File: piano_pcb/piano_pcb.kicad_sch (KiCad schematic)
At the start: 13 parts, among them J1 DIN-6, J2 DIN-6, U1 TB6612FNG

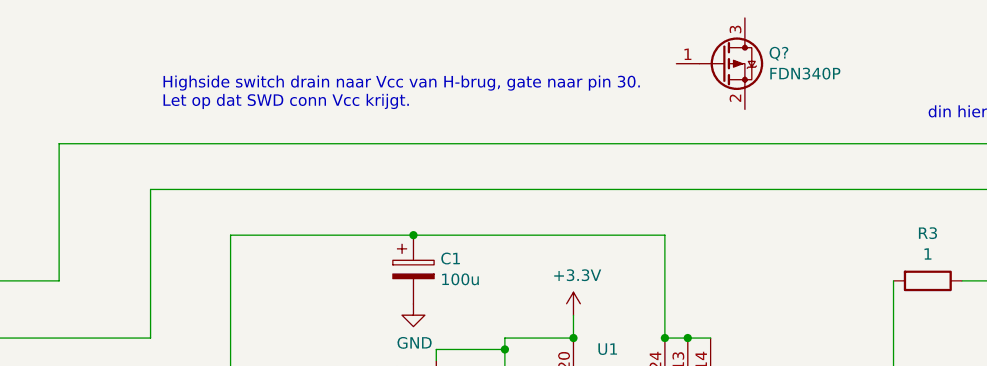
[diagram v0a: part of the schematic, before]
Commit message: Improved low power behaviour
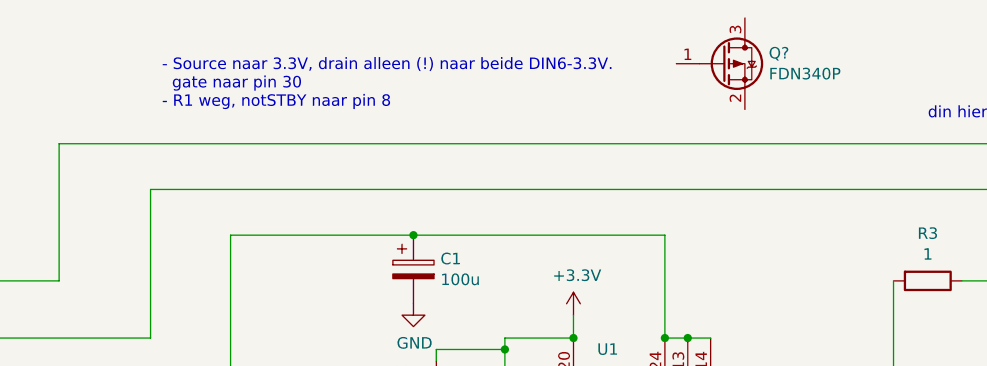
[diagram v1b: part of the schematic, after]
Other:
- note added: "- Source naar 3.3V, drain alleen (!) naar beide DIN6-3.3V. gate naar pin 30 - R1 weg, notSTBY naar pin 8"
- note removed: "Highside switch drain naar Vcc van H-brug, gate naar pin 30. Let op dat SWD conn Vcc krijgt."
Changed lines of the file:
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@@
     (effects (font (size 1.27 1.27)) (justify left bottom))
   )
-  (text "Highside switch drain naar Vcc van H-brug, gate naar pin 30.\nLet op dat SWD conn Vcc krijgt."
+  (text "- Source naar 3.3V, drain alleen (!) naar beide DIN6-3.3V.\n  gate naar pin 30\n- R1 weg, notSTBY naar pin 8"
     (at 158.75 25.4 0)
     (effects (font (size 1.27 1.27)) (justify left bottom))

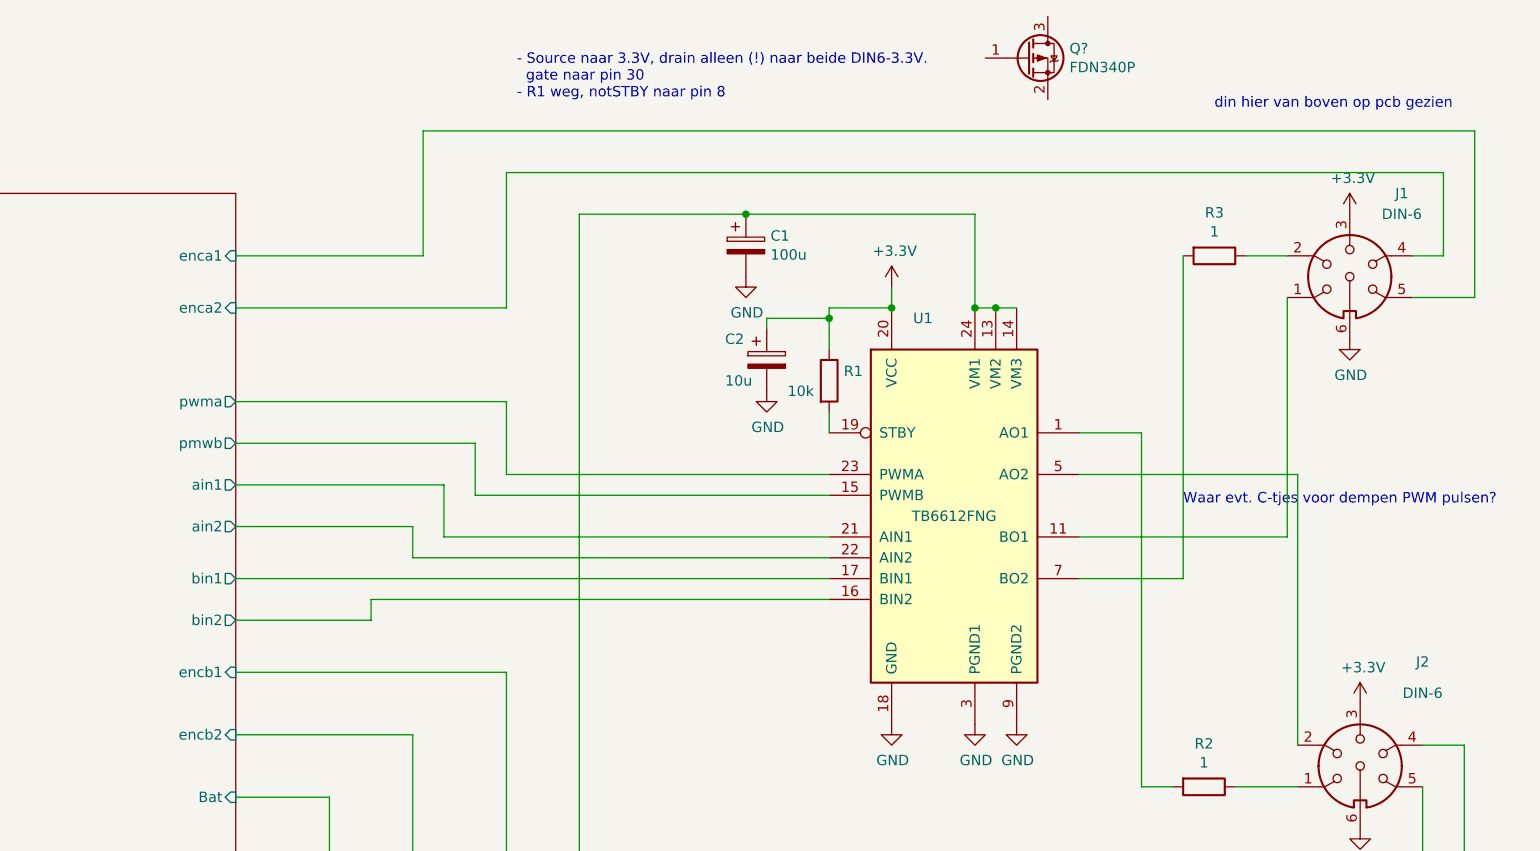
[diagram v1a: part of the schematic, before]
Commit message: Updated schematics, NOT PCB
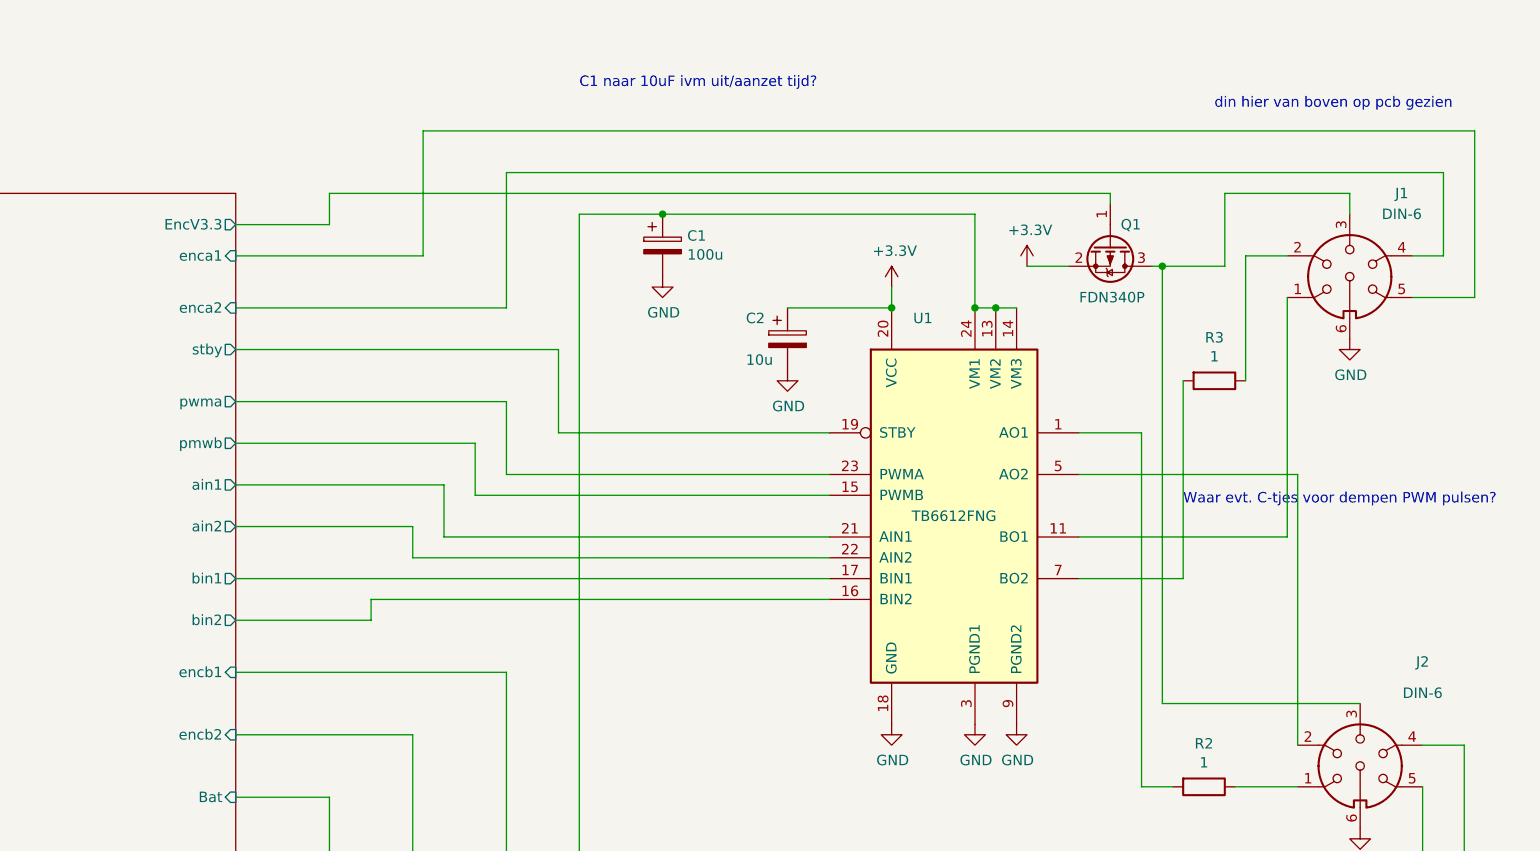
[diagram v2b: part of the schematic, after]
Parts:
- removed R1: 10k, Resistor_SMD:R_0805_2012Metric_Pad1.20x1.40mm_HandSolder, symbol Device:R
- gave numbers to parts that had none: 1
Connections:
- net +3V3: now also Q1.2 (S); no longer J1.3, J2.3
- net Controller/stby: now reaches U1.19 (STBY)
- net Controller/EncV3.3: now reaches Q1.1 (G)
- net at Q1.3 (D): now also J1.3, J2.3
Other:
- sheet Controller ports: added EncV3.3, stby; removed none
- note added: "C1 naar 10uF ivm uit/aanzet tijd?"
- note removed: "- Source naar 3.3V, drain alleen (!) naar beide DIN6-3.3V. gate naar pin 30 - R1 weg, notSTBY naar pin 8"
- moved on the sheet: C1, C2, Q1, R3

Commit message: Minor updates
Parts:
- C1: value 100u -> 10u
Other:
- note added: "Aan welke kant moet de USB plug?"
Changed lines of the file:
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@@
+    (effects (font (size 1.27 1.27)) (justify left bottom))
+  )
+  (text "Aan welke kant moet de USB plug?" (at 62.23 24.13 0)
     (effects (font (size 1.27 1.27)) (justify left bottom))
   )
@@
       (effects (font (size 1.27 1.27)) (justify left))
     )
-    (property "Value" "100u" (id 1) (at 179.5272 44.323 0)
+    (property "Value" "10u" (id 1) (at 179.5272 44.323 0)
       (effects (font (size 1.27 1.27)) (justify left))
     )
@@
     )
     (path "/00000000-0000-0000-0000-00006054c04d"
-      (reference "C1") (unit 1) (value "100u") (footprint "Capacitor_Tantalum_SMD:CP_EIA-7343-30_AVX-N_Pad2.25x2.55mm_HandSolder")
+      (reference "C1") (unit 1) (value "10u") (footprint "Capacitor_Tantalum_SMD:CP_EIA-7343-30_AVX-N_Pad2.25x2.55mm_HandSolder")
     )
     (path "/00000000-0000-0000-0000-00006054c997"
@@
       (reference "J6") (unit 1) (value "Conn_02x01") (footprint "Connector_PinHeader_2.54mm:PinHeader_1x02_P2.54mm_Vertical")
     )
+    (path "/00000000-0000-0000-0000-00006048eab7/0ba958be-8911-456e-aad0-fe6eb7697cab"
+      (reference "J7") (unit 1) (value "Conn_01x02") (footprint "TerminalBlock_Altech:Altech_AK300_1x02_P5.00mm_45-Degree")
+    )
     (path "/00000000-0000-0000-0000-0000632247d1"

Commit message: Optimized for low power
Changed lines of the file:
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@@
 (kicad_sch
-	(version 20231120)
+	(version 20250114)
 	(generator "eeschema")
-	(generator_version "8.0")
+	(generator_version "9.0")
 	(paper "A4")
 	(title_block
@@
 		(comment 4 "Author: Sietse Achterop")
 	)
+	(text "din hier van boven op pcb gezien"
+		(exclude_from_sim no)
+		(at 243.84 26.67 0)
+		(effects
+			(font
+				(size 1.27 1.27)
+			)
+			(justify left bottom)
+		)
+	)
+	(text "PAS OP: TB6612 heeft \"hidden\" aansluitingen: 2 (naast 1),  6,  8, 12\n              Hoe heb ik die nu aangesloten in de layout?\n              Anders doen!!!"
+		(exclude_from_sim no)
+		(at 171.45 137.16 0)
+		(effects
+			(font
+				(size 1.27 1.27)
+			)
+			(justify left bottom)
+		)
+	)
+	(text "C1 naar 10uF ivm uit/aanzet tijd?"
+		(exclude_from_sim no)
+		(at 166.37 24.13 0)
+		(effects
+			(font
+				(size 1.27 1.27)
+			)
+			(justify left bottom)
+		)
+	)
+	(text "Aan welke kant moet de USB plug?"
+		(exclude_from_sim no)
+		(at 62.23 24.13 0)
+		(effects
+			(font
+				(size 1.27 1.27)
+			)
+			(justify left bottom)
+		)
+	)
+	(text "Waar evt. C-tjes voor dempen PWM pulsen?"
+		(exclude_from_sim no)
+		(at 240.03 74.93 0)
+		(effects
+			(font
+				(size 1.27 1.27)
+			)
+			(justify left bottom)
+		)
+	)
 	(junction
 		(at 214.63 50.8)
@@
 			(width 0)
 			(type default)
-		)
-	)
-	(text "din hier van boven op pcb gezien"
-		(exclude_from_sim no)
-		(at 243.84 26.67 0)
-		(effects
-			(font
-				(size 1.27 1.27)
-			)
-			(justify left bottom)
-		)
-	)
-	(text "PAS OP: TB6612 heeft \"hidden\" aansluitingen: 2 (naast 1),  6,  8, 12\n              Hoe heb ik die nu aangesloten in de layout?\n              Anders doen!!!"
-		(exclude_from_sim no)
-		(at 171.45 137.16 0)
-		(effects
-			(font
-				(size 1.27 1.27)
-			)
-			(justify left bottom)
-		)
-	)
-	(text "C1 naar 10uF ivm uit/aanzet tijd?"
-		(exclude_from_sim no)
-		(at 166.37 24.13 0)
-		(effects
-			(font
-				(size 1.27 1.27)
-			)
-			(justify left bottom)
-		)
-	)
-	(text "Aan welke kant moet de USB plug?"
-		(exclude_from_sim no)
-		(at 62.23 24.13 0)
-		(effects
-			(font
-				(size 1.27 1.27)
-			)
-			(justify left bottom)
-		)
-	)
-	(text "Waar evt. C-tjes voor dempen PWM pulsen?"
-		(exclude_from_sim no)
-		(at 240.03 74.93 0)
-		(effects
-			(font
-				(size 1.27 1.27)
-			)
-			(justify left bottom)
 		)
 	)
@@
 		(at 36.83 137.16)
 		(size 57.15 31.75)
+		(exclude_from_sim no)
+		(in_bom yes)
+		(on_board yes)
+		(dnp no)
 		(fields_autoplaced yes)
 		(stroke
@@
 		(at 49.53 36.83)
 		(size 74.93 81.28)
+		(exclude_from_sim no)
+		(in_bom yes)
+		(on_board yes)
+		(dnp no)
 		(fields_autoplaced yes)
 		(stroke
@@
 		)
 	)
+	(embedded_fonts no)
 )

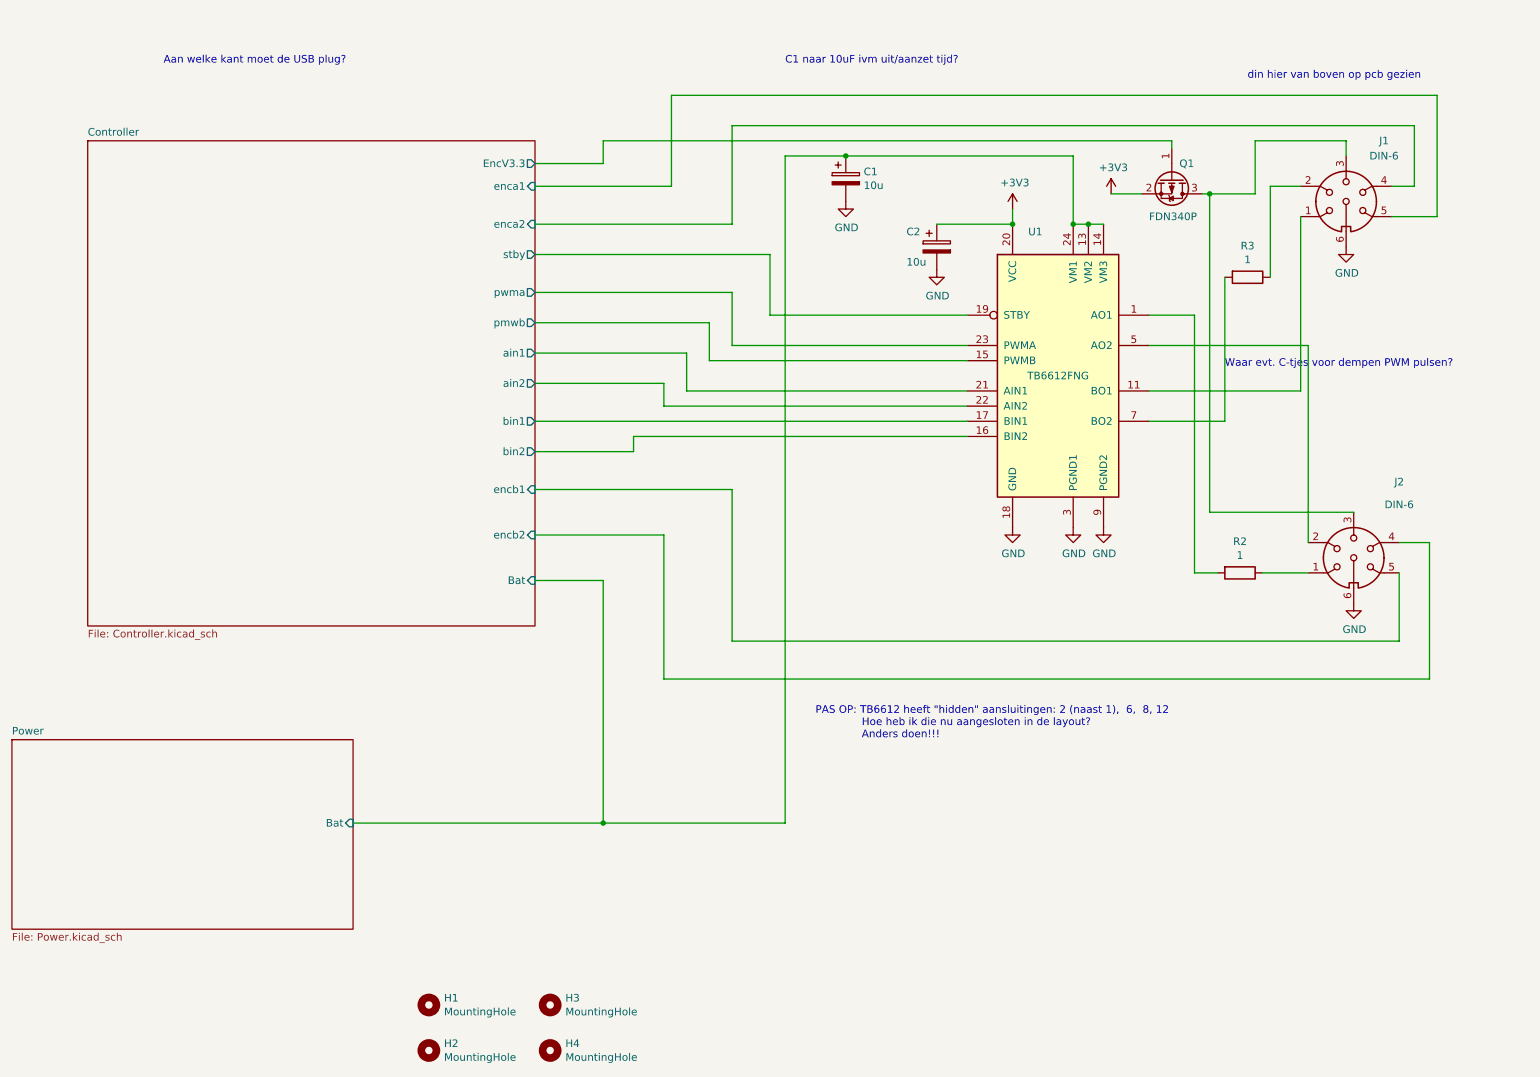
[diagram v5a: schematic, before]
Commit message: PCB to version 2.0
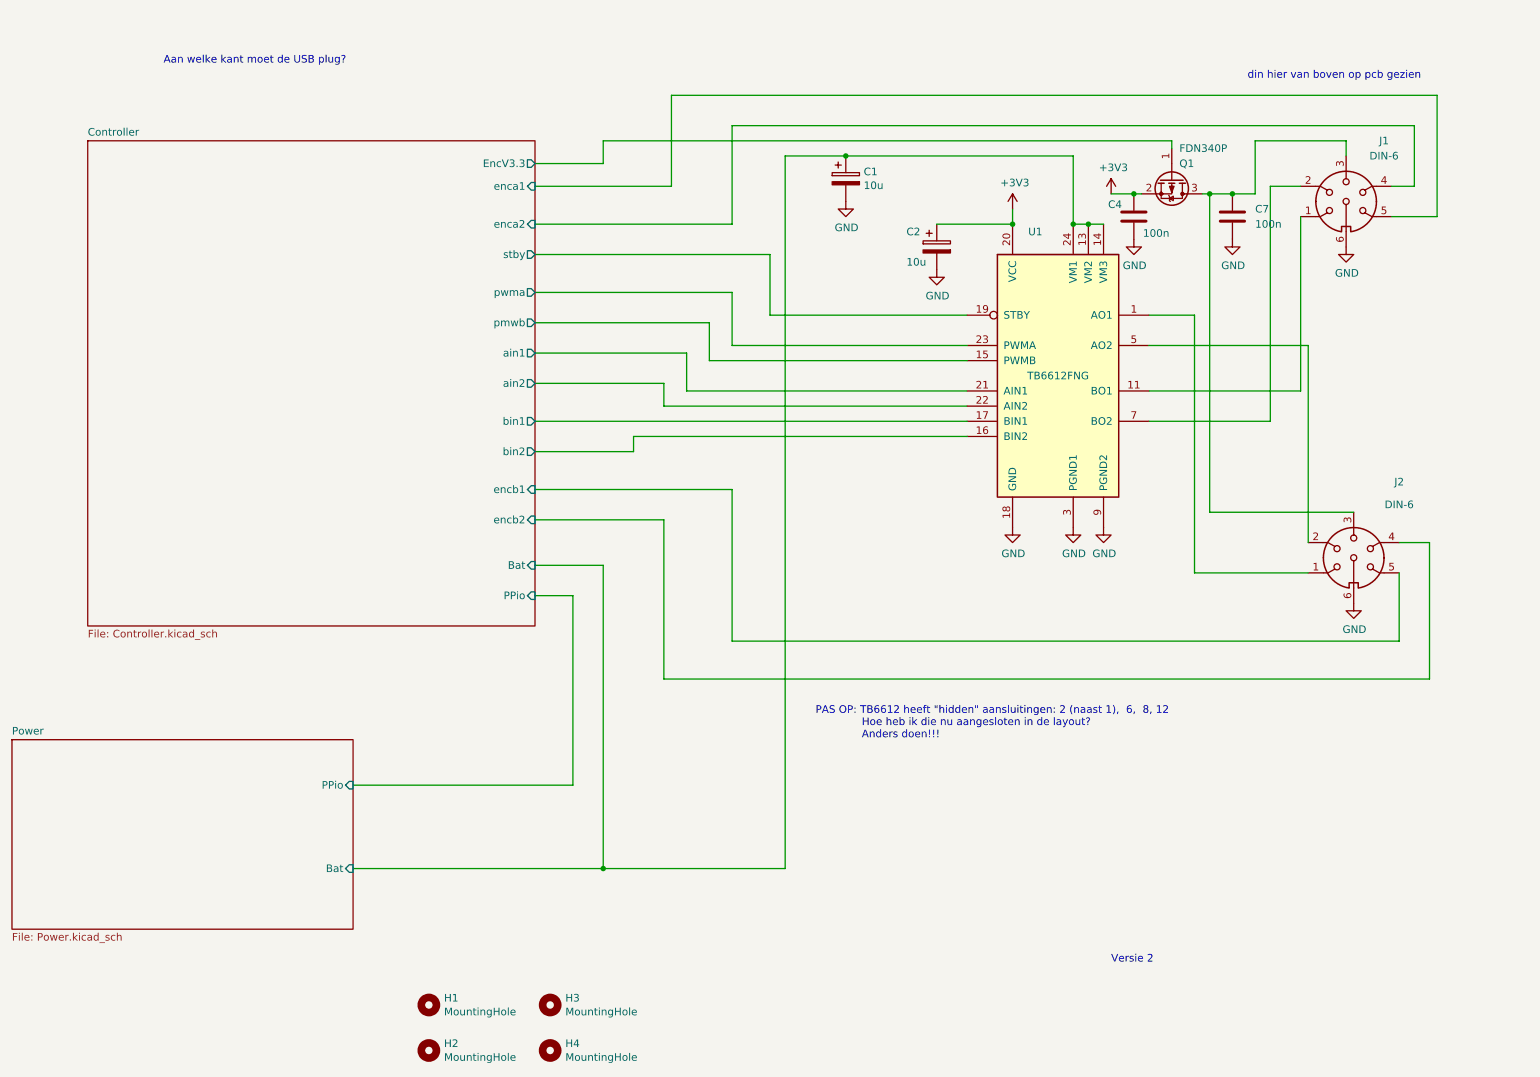
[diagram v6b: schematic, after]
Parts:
- removed R2, R3: 1, Resistor_THT:R_Axial_Power_L20.0mm_W6.4mm_P5.08mm_Vertical, symbol Device:R
- added C4, C7: 100n, Capacitor_SMD:C_1210_3225Metric_Pad1.33x2.70mm_HandSolder, symbol Device:C
- C1: footprint Capacitor_Tantalum_SMD:CP_EIA-7343-30_AVX-N_Pad2.25x2.55mm_HandSolder -> Capacitor_Tantalum_SMD:CP_EIA-7343-30_AVX-N_HandSolder
- J1, J2: footprint myAV:din-6-1cm -> library:din-6-1cm
- U1: footprint myAV:SSOP-24_5.3x8.2mm_P0.65mm -> library:SSOP-24_5.3x8.2mm_P0.65mm
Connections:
- net +3V3: now also C4.1
- net GND: now also C4.2, C7.2
- net at U1.1 (AO1), U1.2 (AO1): now also J2.1
- net at U1.7 (BO2), U1.8 (BO2): now also J1.2
- net at J1.3, J2.3, Q1.3 (D): now also C7.1
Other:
- sheet Controller ports: added PPio; removed none
- sheet Power ports: added PPio; removed none
- note added: "Versie 2"
- note removed: "C1 naar 10uF ivm uit/aanzet tijd?"
- note removed: "Waar evt. C-tjes voor dempen PWM pulsen?"
